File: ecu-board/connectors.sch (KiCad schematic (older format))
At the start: 37 parts, among them J10 Injector connector, J11 Cockpit connector, J12 EGO connector, J13 Chrankshaft Hall connector, J14 Camshaft Hall connector, J15 Ignition 1 connector, J16 Ignition 2 connector, J17 Camera connector, J18 Wheel Hall connector, J2 Battery power conenctor, J4 Motor connector, J5 Serial DB9 connector, J6 Controller connector, J7 Backlight connector, J8 IAT connector, J9 CLT connector

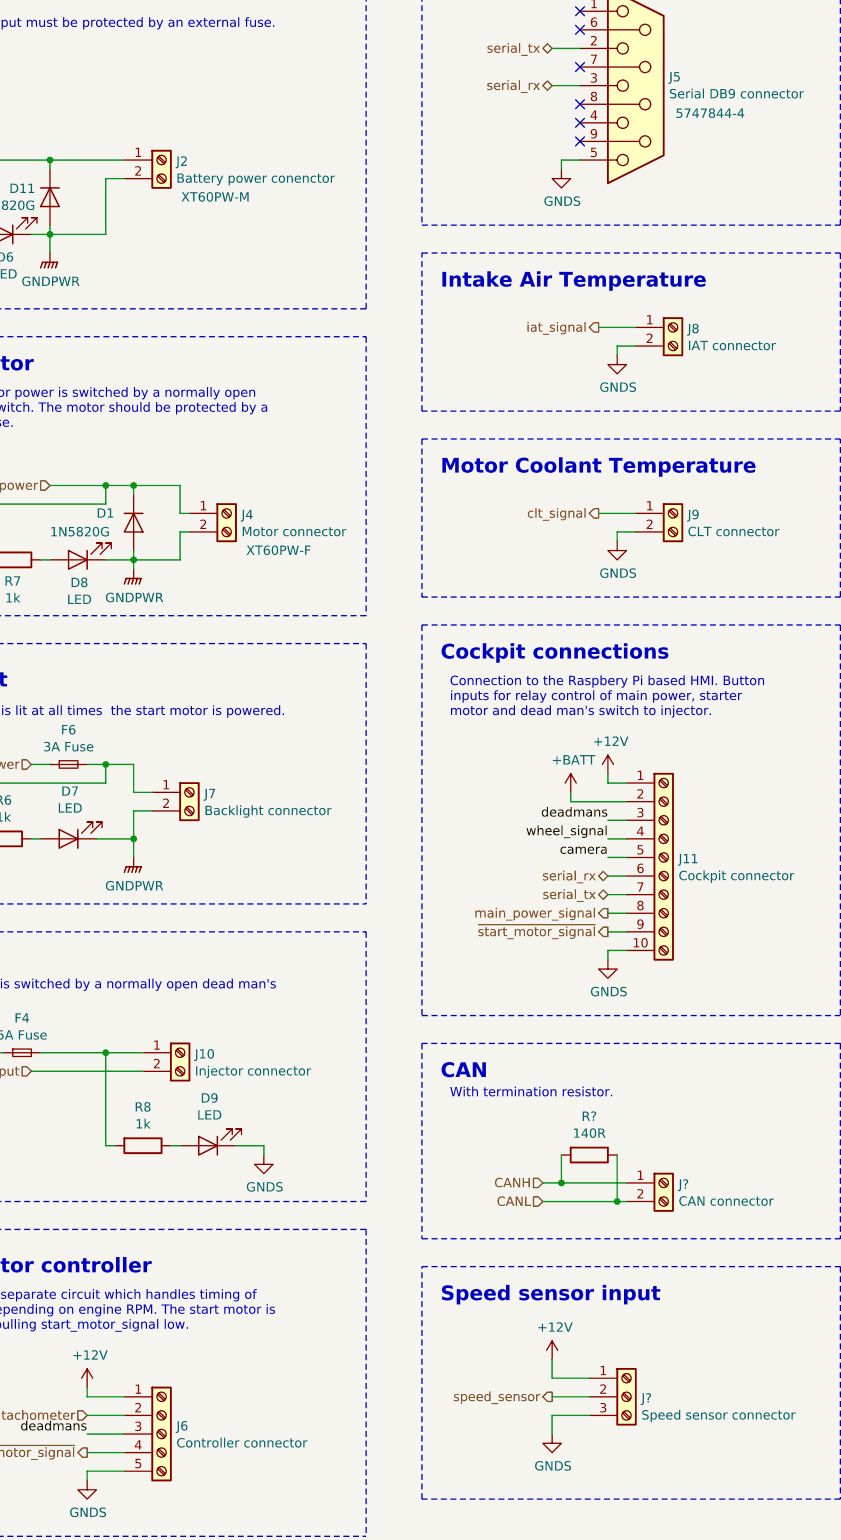
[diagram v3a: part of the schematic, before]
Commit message: Start power circuit routing.
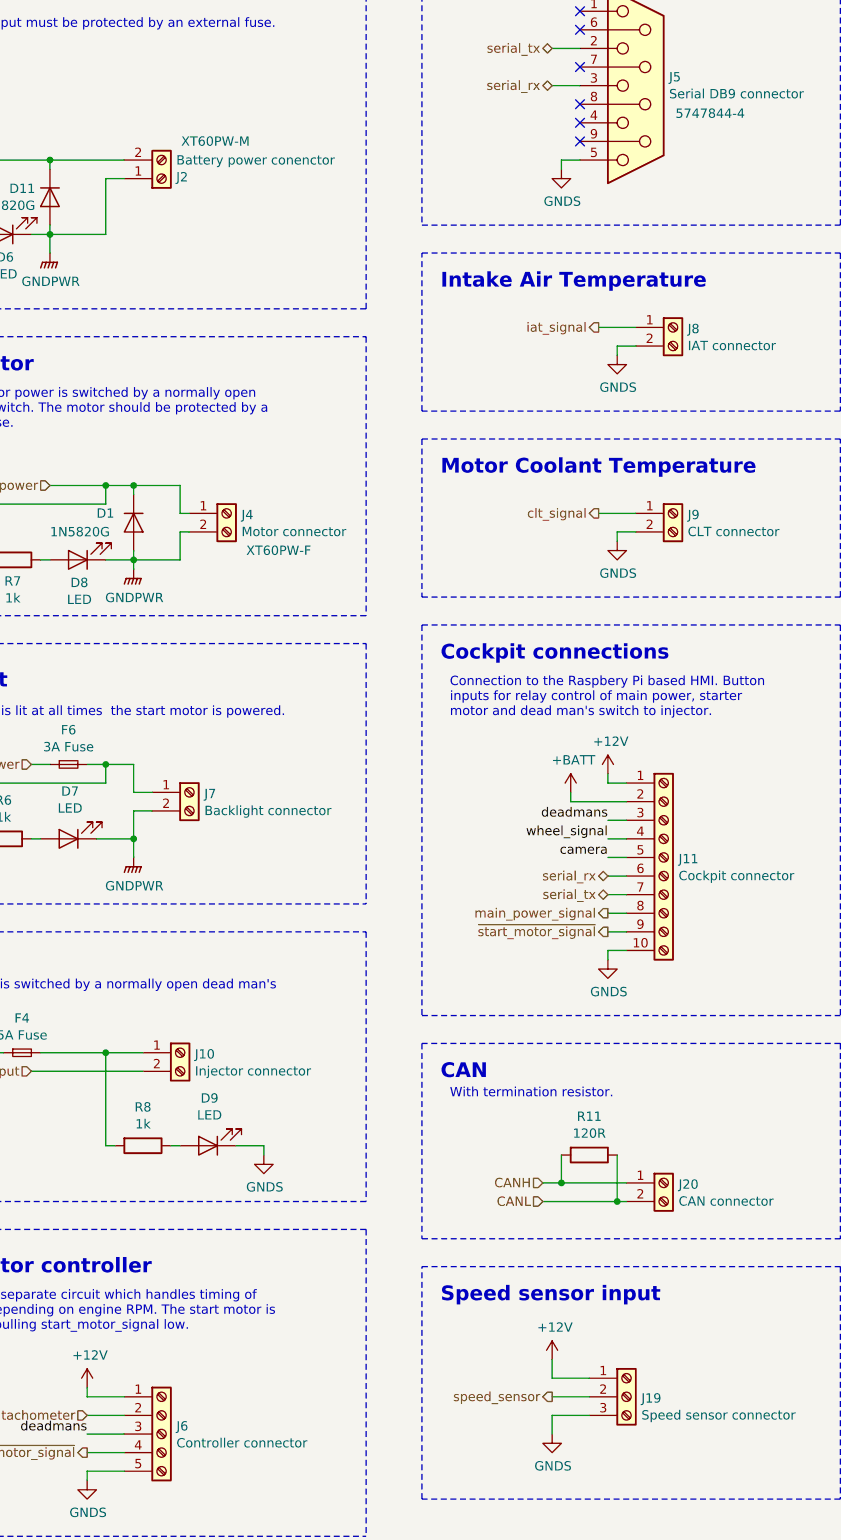
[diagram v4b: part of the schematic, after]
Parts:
- R11: renamed from R?; value 140R -> 120R; footprint (none) -> Resistors_SMD:R_0805_HandSoldering
- gave numbers to parts that had none: 2
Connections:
- net +BATT: now also J2.2 (Pin_2); no longer J2.1 (Pin_1)
- net GNDPWR: now also J2.1 (Pin_1); no longer J2.2 (Pin_2)
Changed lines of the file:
@@
 Sheet 3 3
 Title "Vera ECU Board"
-Date "2019-07-07"
+Date "2019-09-29"
 Rev "0.1"
 Comp "Chalmers Vera Team"
@@
 L Connector:Screw_Terminal_01x02 J2
 U 1 1 5C5C3CF5
-P 2300 2300
-F 0 "J2" H 2379 2292 50  0000 L CNN
-F 1 "Battery power conenctor" H 2379 2201 50  0000 L CNN
-F 2 "ecu-board-footprints:AMASS_XT60PW" H 2300 2300 50  0001 C CNN
-F 3 "~" H 2300 2300 50  0001 C CNN
-F 4 "AMASS" H 2300 2300 50  0001 C CNN "Manufacturer"
-F 5 "XT60PW-M" H 2590 2100 50  0000 C CNN "Part no."
-	1    2300 2300
-	1    0    0    -1
+P 2300 2400
+F 0 "J2" H 2379 2392 50  0000 L CNN
+F 1 "Battery power conenctor" H 2379 2301 50  0000 L CNN
+F 2 "ecu-board-footprints:AMASS_XT60PW" H 2300 2400 50  0001 C CNN
+F 3 "~" H 2300 2400 50  0001 C CNN
+F 4 "AMASS" H 2300 2400 50  0001 C CNN "Manufacturer"
+F 5 "XT60PW-M" H 2590 2200 50  0000 C CNN "Part no."
+	1    2300 2400
+	1    0    0    1
 $EndComp
 $Comp
@@
 Speed sensor input
 $Comp
-L Connector:Screw_Terminal_01x03 J?
+L Connector:Screw_Terminal_01x03 J19
 U 1 1 5DA598D9
 P 4800 8950
-F 0 "J?" H 4880 8942 50  0000 L CNN
+F 0 "J19" H 4880 8942 50  0000 L CNN
 F 1 "Speed sensor connector" H 4880 8851 50  0000 L CNN
 F 2 "ecu-board-footprints:Terminal_Block_3x5.00mm" H 4800 8950 50  0001 C CNN
@@
 $EndComp
 $Comp
-L power:GNDS #PWR?
+L power:GNDS #PWR051
 U 1 1 5DA6AA4C
 P 4400 9150
-F 0 "#PWR?" H 4400 8900 50  0001 C CNN
+F 0 "#PWR051" H 4400 8900 50  0001 C CNN
 F 1 "GNDS" H 4405 8977 50  0000 C CNN
 F 2 "" H 4400 9150 50  0001 C CNN
@@
 $EndComp
 $Comp
-L power:+12V #PWR?
+L power:+12V #PWR050
 U 1 1 5DA6B84B
 P 4400 8750
-F 0 "#PWR?" H 4400 8600 50  0001 C CNN
+F 0 "#PWR050" H 4400 8600 50  0001 C CNN
 F 1 "+12V" H 4415 8923 50  0000 C CNN
 F 2 "" H 4400 8750 50  0001 C CNN
@@
 	4450 7650 4450 7800
 $Comp
-L Device:R R?
+L Device:R R11
 U 1 1 5DAC1E2A
 P 4600 7650
-F 0 "R?" V 4393 7650 50  0000 C CNN
-F 1 "140R" V 4484 7650 50  0000 C CNN
-F 2 "" V 4530 7650 50  0001 C CNN
+F 0 "R11" V 4393 7650 50  0000 C CNN
+F 1 "120R" V 4484 7650 50  0000 C CNN
+F 2 "Resistors_SMD:R_0805_HandSoldering" V 4530 7650 50  0001 C CNN
 F 3 "~" H 4600 7650 50  0001 C CNN
 	1    4600 7650
@@
 CANH
 $Comp
-L Connector:Screw_Terminal_01x02 J?
+L Connector:Screw_Terminal_01x02 J20
 U 1 1 5D94B35C
 P 5000 7800
-F 0 "J?" H 5080 7792 50  0000 L CNN
+F 0 "J20" H 5080 7792 50  0000 L CNN
 F 1 "CAN connector" H 5080 7701 50  0000 L CNN
 F 2 "ecu-board-footprints:Terminal_Block_2x5.00mm" H 5000 7800 50  0001 C CNN

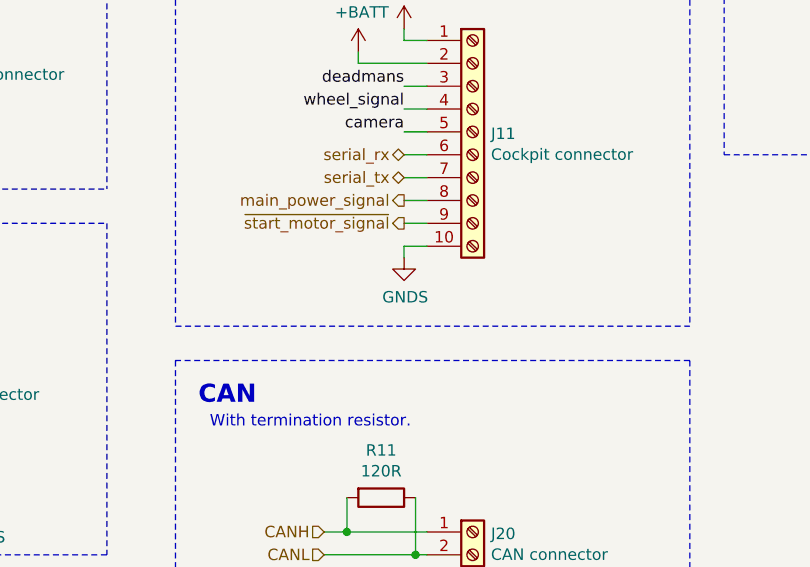
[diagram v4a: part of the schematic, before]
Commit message: Change cockpit ground from SGND to PWRGND.
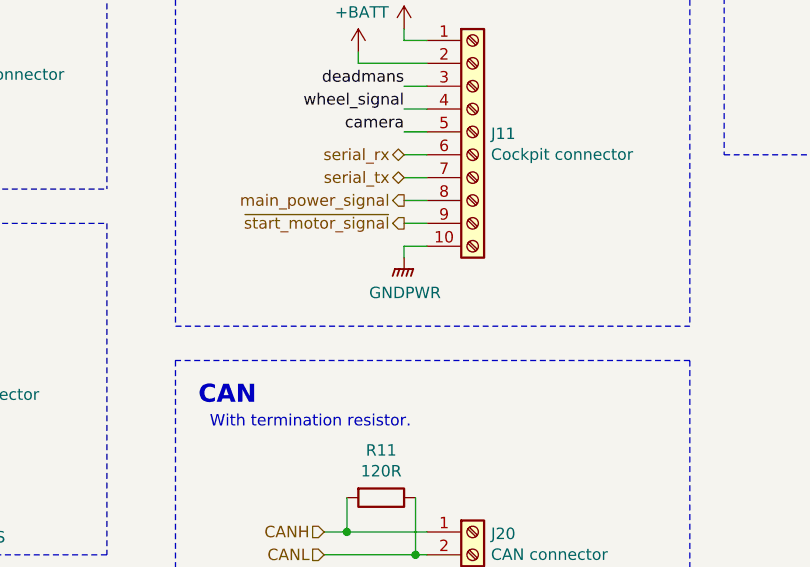
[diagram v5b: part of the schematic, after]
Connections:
- net GNDPWR: now also J11.10 (Pin_10)
- net GNDS: no longer J11.10 (Pin_10)
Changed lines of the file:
@@
-	1    0    0    -1
-$EndComp
-$Comp
-L power:GNDS #PWR025
-U 1 1 5C66C0AC
-P 4700 6600
-F 0 "#PWR025" H 4700 6350 50  0001 C CNN
-F 1 "GNDS" H 4705 6427 50  0000 C CNN
-F 2 "" H 4700 6600 50  0001 C CNN
-F 3 "" H 4700 6600 50  0001 C CNN
-	1    4700 6600
 	1    0    0    -1
 $EndComp
@@
 	1    0    0    -1
 $EndComp
+$Comp
+L power:GNDPWR #PWR?
+U 1 1 5DA363EE
+P 4700 6600
+F 0 "#PWR?" H 4700 6400 50  0001 C CNN
+F 1 "GNDPWR" H 4704 6446 50  0000 C CNN
+F 2 "" H 4700 6550 50  0001 C CNN
+F 3 "" H 4700 6550 50  0001 C CNN
+	1    4700 6600
+	1    0    0    -1
+$EndComp

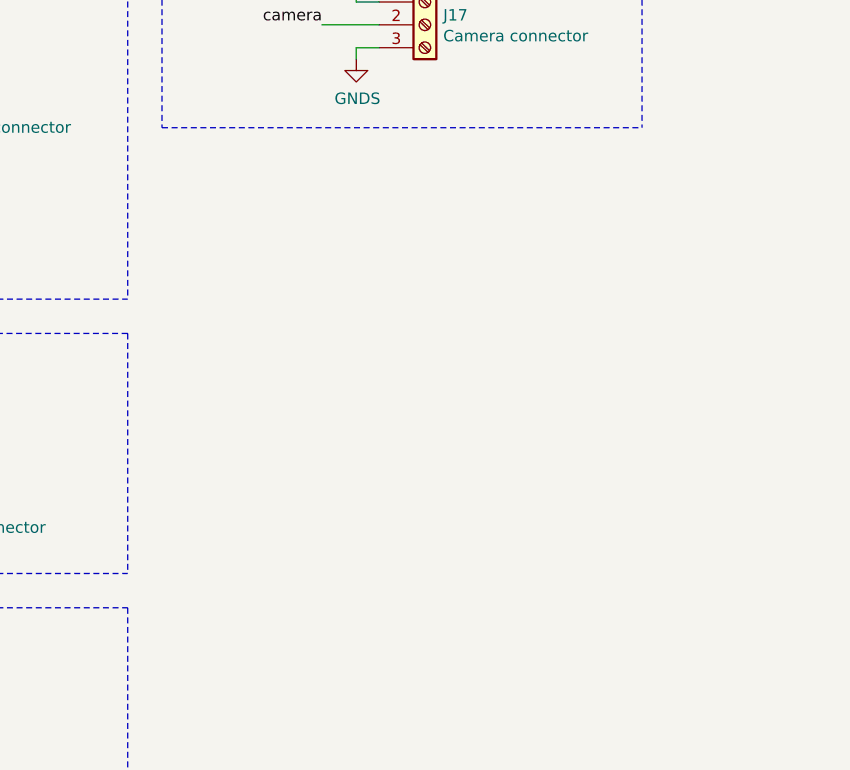
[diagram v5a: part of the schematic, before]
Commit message: Add redundant 12V and PWRGND connectors. Closes #52. Also add PWRGND copper pour.
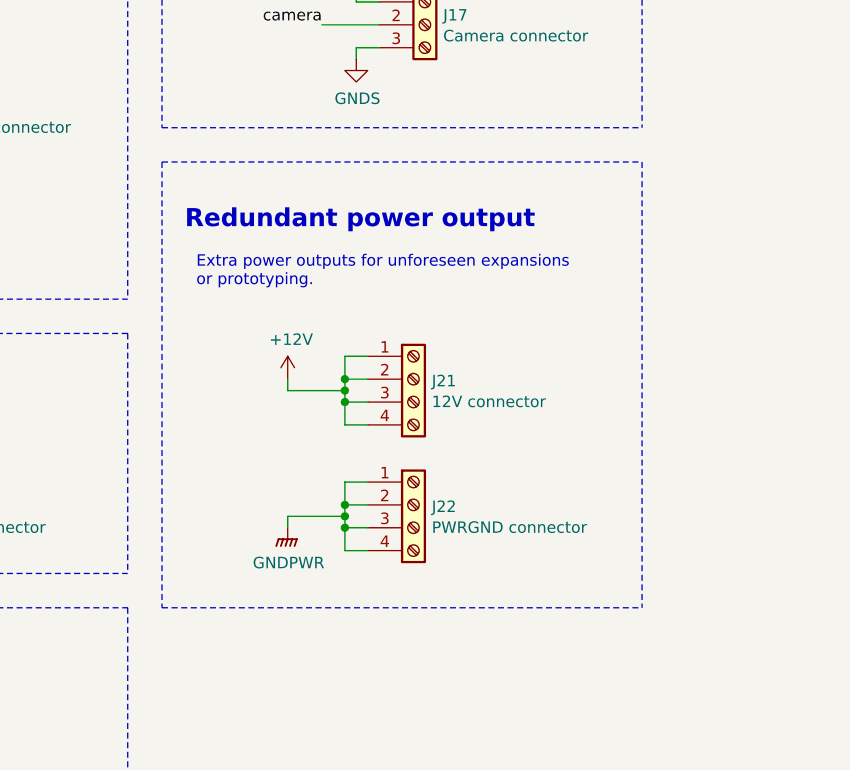
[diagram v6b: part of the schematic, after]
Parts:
- added J21: 12V connector, ecu-board-footprints:Terminal_Block_4x5.00mm, symbol Connector:Screw_Terminal_01x04
- added J22: PWRGND connector, ecu-board-footprints:Terminal_Block_4x5.00mm, symbol Connector:Screw_Terminal_01x04
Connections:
- net +12V: now also J21.1 (Pin_1), J21.2 (Pin_2), J21.3 (Pin_3), J21.4 (Pin_4)
- net GNDPWR: now also J22.1 (Pin_1), J22.2 (Pin_2), J22.3 (Pin_3), J22.4 (Pin_4)
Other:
- note added: "Extra power outputs for unforeseen expansions \nor prototyping."
- note added: "Redundant power output"
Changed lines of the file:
@@
 $EndComp
 $Comp
-L power:GNDPWR #PWR?
+L power:GNDPWR #PWR0102
 U 1 1 5DA363EE
 P 4700 6600
-F 0 "#PWR?" H 4700 6400 50  0001 C CNN
+F 0 "#PWR0102" H 4700 6400 50  0001 C CNN
 F 1 "GNDPWR" H 4704 6446 50  0000 C CNN
 F 2 "" H 4700 6550 50  0001 C CNN
@@
 	1    0    0    -1
 $EndComp
+Text Notes 6200 6600 0    79   ~ 16
+Redundant power output
+Wire Notes Line
+	6100 6300 8200 6300
+$Comp
+L Connector:Screw_Terminal_01x04 J21
+U 1 1 5DA58887
+P 7200 7250
+F 0 "J21" H 7280 7242 50  0000 L CNN
+F 1 "12V connector" H 7280 7151 50  0000 L CNN
+F 2 "ecu-board-footprints:Terminal_Block_4x5.00mm" H 7200 7250 50  0001 C CNN
+F 3 "~" H 7200 7250 50  0001 C CNN
+F 4 "Würth" H 7200 7250 50  0001 C CNN "Manufacturer"
+F 5 "2141 Series" H 7200 7250 50  0001 C CNN "Part no."
+	1    7200 7250
+	1    0    0    -1
+$EndComp
+$Comp
+L Connector:Screw_Terminal_01x04 J22
+U 1 1 5DA5ABE7
+P 7200 7800
+F 0 "J22" H 7280 7792 50  0000 L CNN
+F 1 "PWRGND connector" H 7280 7701 50  0000 L CNN
+F 2 "ecu-board-footprints:Terminal_Block_4x5.00mm" H 7200 7800 50  0001 C CNN
+F 3 "~" H 7200 7800 50  0001 C CNN
+F 4 "Würth" H 7200 7800 50  0001 C CNN "Manufacturer"
+F 5 "2141 Series" H 7200 7800 50  0001 C CNN "Part no."
+	1    7200 7800
+	1    0    0    -1
+$EndComp
+Text Notes 6250 6850 0    50   ~ 0
+Extra power outputs for unforeseen expansions \nor prototyping.
+$Comp
+L power:GNDPWR #PWR028
+U 1 1 5DA5D5C4
+P 6650 7900
+F 0 "#PWR028" H 6650 7700 50  0001 C CNN
+F 1 "GNDPWR" H 6654 7746 50  0000 C CNN
+F 2 "" H 6650 7850 50  0001 C CNN
+F 3 "" H 6650 7850 50  0001 C CNN
+	1    6650 7900
+	1    0    0    -1
+$EndComp
+Wire Wire Line
+	6650 7900 6650 7850
+Wire Wire Line
+	6650 7850 6900 7850
+Wire Wire Line
+	6900 7850 6900 7800
+Wire Wire Line
+	6900 7700 7000 7700
+Wire Wire Line
+	6900 7850 6900 7900
+Wire Wire Line
+	6900 8000 7000 8000
+Connection ~ 6900 7850
+Wire Wire Line
+	7000 7900 6900 7900
+Connection ~ 6900 7900
+Wire Wire Line
+	6900 7900 6900 8000
+Wire Wire Line
+	7000 7800 6900 7800
+Connection ~ 6900 7800
+Wire Wire Line
+	6900 7800 6900 7700
+$Comp
+L power:+12V #PWR025
+U 1 1 5DA85A09
+P 6650 7250
+F 0 "#PWR025" H 6650 7100 50  0001 C CNN
+F 1 "+12V" H 6665 7423 50  0000 C CNN
+F 2 "" H 6650 7250 50  0001 C CNN
+F 3 "" H 6650 7250 50  0001 C CNN
+	1    6650 7250
+	1    0    0    -1
+$EndComp
+Wire Wire Line
+	6650 7250 6650 7300
+Wire Wire Line
+	6650 7300 6900 7300
+Wire Wire Line
+	6900 7300 6900 7250
+Wire Wire Line
+	6900 7150 7000 7150
+Wire Wire Line
+	7000 7450 6900 7450
+Wire Wire Line
+	6900 7450 6900 7350
+Connection ~ 6900 7300
+Wire Wire Line
+	7000 7350 6900 7350
+Connection ~ 6900 7350
+Wire Wire Line
+	6900 7350 6900 7300
+Wire Wire Line
+	6900 7250 7000 7250
+Connection ~ 6900 7250
+Wire Wire Line
+	6900 7250 6900 7150
+Wire Notes Line
+	6100 8250 8200 8250
+Wire Notes Line
+	8200 6300 8200 8250
+Wire Notes Line
+	6100 6300 6100 8250
 $EndSCHEMATC
